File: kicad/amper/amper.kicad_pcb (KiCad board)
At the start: 2 copper layers, 45 parts, among them J1 Conn_01x05, J2 Conn_01x02, J3 Conn_01x15, J4 Conn_01x10, J5 Conn_01x10, Q1 FDS9435A, Q2 FDS9435A, SW1 SW_Push, SW2 SW_Push, SW3 SW_Push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

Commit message: amper rev a
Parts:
- added svg2mod: G***, amper:iridyne_logo, B.Cu at (97.5, 28.6)
- added svg2mod: G***, amper:iridyne_logo, F.Cu at (97.5, 28.6)
- U1: value TM1637 -> UA741CP; footprint amper:TM1637 -> amper:114-87-308-41-134161
- U5: value UA741CP -> TM1637; footprint amper:114-87-308-41-134161 -> amper:TM1637
- moved TP1 162.8 mm to (27.2, 20.9)
- moved R9 153.8 mm to (34.5, 18.6)
- moved R7 153.5 mm to (34.5, 20.9), turned to 180 degrees
- moved TP3 151.2 mm to (35.4, 16.1)
- moved TP5 149.6 mm to (44.3, 16.1)
- moved R6 149.3 mm to (30.1, 59.1), turned to 270 degrees
- moved C5 148.6 mm to (34.5, 25.5), turned to 180 degrees
- moved TP2 148.3 mm to (27.2, 36.1)
- moved C2 146.8 mm to (31.8, 59.1), turned to 90 degrees
- moved TP4 146.1 mm to (35.4, 31.3)
- moved R13 144.4 mm to (46.6, 21.1), turned to 270 degrees
- moved TP6 143.8 mm to (44.3, 31.3)
- moved C6 143.3 mm to (34.5, 40.7), turned to 180 degrees
- moved R10 141.0 mm to (34.5, 23.2), turned to 180 degrees
- moved R8 140.5 mm to (34.5, 36.1), turned to 180 degrees
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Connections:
- SW1 pad 1: /SourceBUp -> /SourceAUp
- SW2 pad 1: /SourceBDn -> /SourceADn
- SW3 pad 1: /SourceAUp -> /SourceBUp
- SW4 pad 1: /SourceADn -> /SourceBDn
- U1 pad 1: GND -> Net-(U1-Pad1)
- U1 pad 2: /SEG1 -> Net-(J2-Pad2)
- U1 pad 3: /SEG2 -> Net-(J2-Pad1)
- U1 pad 4: /SEG3 -> GND
- U1 pad 5: /SEG4 -> Net-(U1-Pad5)
- U1 pad 6: /SEG5 -> /AmpOut
- U1 pad 7: /SEG6 -> +5V
- U1 pad 8: /SEG7 -> Net-(U1-Pad8)
- U3 pad 10: /SourceBDigit1 -> /SourceADigit1
- U3 pad 5: /SourceBDigit2 -> /SourceADigit2
- U4 pad 10: /SourceADigit1 -> /SourceBDigit1
- U4 pad 5: /SourceADigit2 -> /SourceBDigit2
- U5 pad 1: Net-(U5-Pad1) -> GND
- U5 pad 2: Net-(J2-Pad1) -> /SEG1
- U5 pad 3: Net-(J2-Pad2) -> /SEG2
- U5 pad 4: GND -> /SEG3
- U5 pad 5: Net-(U5-Pad5) -> /SEG4
- U5 pad 6: /AmpOut -> /SEG5
- U5 pad 7: +5V -> /SEG6
- U5 pad 8: Net-(U5-Pad8) -> /SEG7
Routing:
- net GND: track 0.00 -> 302.6 mm, vias 0 -> 8
- net +5V: track 0.00 -> 272.9 mm, vias 0 -> 9
- net /SourceA: track 0.00 -> 239.8 mm, vias 0 -> 1
- net /SourceB: track 0.00 -> 194.2 mm, vias 0 -> 1
- net /SEG4: track 0.00 -> 166.4 mm, vias 0 -> 4
- net /AmpOut: track 0.00 -> 165.8 mm
- net /SEG3: track 0.00 -> 163.5 mm, vias 0 -> 4
- net /SEG2: track 0.00 -> 161.2 mm, vias 0 -> 4
- net /SEG1: track 0.00 -> 157.7 mm, vias 0 -> 4
- net /SEG8: track 0.00 -> 151.3 mm, vias 0 -> 4
- net /SEG7: track 0.00 -> 151.0 mm, vias 0 -> 4
- net /SEG6: track 0.00 -> 149.2 mm, vias 0 -> 4
- net /SEG5: track 0.00 -> 148.1 mm, vias 0 -> 4
- net /SourceAPWM: track 0.00 -> 142.8 mm, vias 0 -> 1
- net /SourceBDigit1: track 0.00 -> 130.2 mm, vias 0 -> 2
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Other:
- board outline added: 91.4 x 91.4 mm
- board text added: "5V"
- board text added: "A"
- board text added: "ADn"
- board text added: "APwm"
- board text added: "AUp"
- board text added: "Amper Rev A"
- board text added: "B"
- board text added: "BDn"
- board text added: "BPwm"
- board text added: "BUp"
- board text added: "CLK"
- board text added: "DIO"
- board text added: "GND"
- board text added: "Out"
- board text added: "V"

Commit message: Amper rev A ready to go
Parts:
- removed the svg2mod at (97.5, 28.6) (x2)
- added svg2mod: G***, amper:pcb_logo, B.Cu at (98.0, 28.8)
- added svg2mod: G***, amper:pcb_logo, F.Cu at (98.0, 28.8)
- U1: value UA741CP -> 114-87-308-41-134161

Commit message: Reannotated everything
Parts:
- removed C1, C2: 100pF, Capacitor_SMD:C_0603_1608Metric_Pad1.05x0.95mm_HandSolder
- removed C3: 100nF, Capacitor_SMD:C_0603_1608Metric_Pad1.05x0.95mm_HandSolder
- removed C4: 10uF, Capacitor_SMD:C_0603_1608Metric_Pad1.05x0.95mm_HandSolder
- removed C5, C6, C7, C8: 1u, Capacitor_SMD:C_0603_1608Metric_Pad1.05x0.95mm_HandSolder
- removed J1: Conn_01x05, amper:2.54_2x5_col_ganged
- removed J2: Conn_01x02, amper:2.54_2x5_row_ganged
- removed J3: Conn_01x15, Connector_PinSocket_2.54mm:PinSocket_1x15_P2.54mm_Vertical
- removed J4, J5: Conn_01x10, Connector_PinSocket_2.54mm:PinSocket_1x10_P2.54mm_Vertical
- removed Q1, Q2: FDS9435A, Package_SO:SOIC-8_3.9x4.9mm_P1.27mm
- removed R1, R2, R3, R4, R5, R6: 10K, Resistor_SMD:R_0603_1608Metric_Pad1.05x0.95mm_HandSolder
- removed R10, R12: 40k, Resistor_SMD:R_0603_1608Metric_Pad1.05x0.95mm_HandSolder
- removed R11, R9: 25k, Resistor_SMD:R_0603_1608Metric_Pad1.05x0.95mm_HandSolder
- removed R13, R14: 100K, Resistor_SMD:R_0603_1608Metric_Pad1.05x0.95mm_HandSolder
- removed R7, R8: 60k, Resistor_SMD:R_0603_1608Metric_Pad1.05x0.95mm_HandSolder
- removed SW1, SW2, SW3, SW4: SW_Push, amper:K2-1157SP-I4SW-01
- removed TP1, TP2, TP3, TP4, TP5, TP6: TestPoint, TestPoint:TestPoint_Pad_D2.0mm
- removed U1: 114-87-308-41-134161, amper:114-87-308-41-134161
- removed U2, U3, U4: HDSM-441B, amper:SLS0392FB4A1GD
- removed U5: TM1637, amper:TM1637
- removed U6: ATtiny40-SU, Package_SO:SOIC-20W_7.5x12.8mm_P1.27mm
- removed svg2mod (x2): G***, amper:pcb_logo
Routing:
- net GND: track 302.6 -> 0.00 mm, vias 8 -> 0
- net +5V: track 272.9 -> 0.00 mm, vias 9 -> 0
- net /SourceA: track 239.8 -> 0.00 mm, vias 1 -> 0
- net /SourceB: track 194.2 -> 0.00 mm, vias 1 -> 0
- net /SEG4: track 166.4 -> 0.00 mm, vias 4 -> 0
- net /AmpOut: track 165.8 -> 0.00 mm
- net /SEG3: track 163.5 -> 0.00 mm, vias 4 -> 0
- net /SEG2: track 161.2 -> 0.00 mm, vias 4 -> 0
- net /SEG1: track 157.7 -> 0.00 mm, vias 4 -> 0
- net /SEG8: track 151.3 -> 0.00 mm, vias 4 -> 0
- net /SEG7: track 151.0 -> 0.00 mm, vias 4 -> 0
- net /SEG6: track 149.2 -> 0.00 mm, vias 4 -> 0
- net /SEG5: track 148.1 -> 0.00 mm, vias 4 -> 0
- net /SourceAPWM: track 142.8 -> 0.00 mm, vias 1 -> 0
- net /SourceBDigit1: track 130.2 -> 0.00 mm, vias 2 -> 0
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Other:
- board size 91.4 x 91.4 mm -> 100 x 100 mm
- board text removed: "5V"
- board text removed: "A"
- board text removed: "ADn"
- board text removed: "APwm"
- board text removed: "AUp"
- board text removed: "Amper Rev A"
- board text removed: "B"
- board text removed: "BDn"
- board text removed: "BPwm"
- board text removed: "BUp"
- board text removed: "CLK"
- board text removed: "DIO"
- board text removed: "GND"
- board text removed: "Out"
- board text removed: "V"

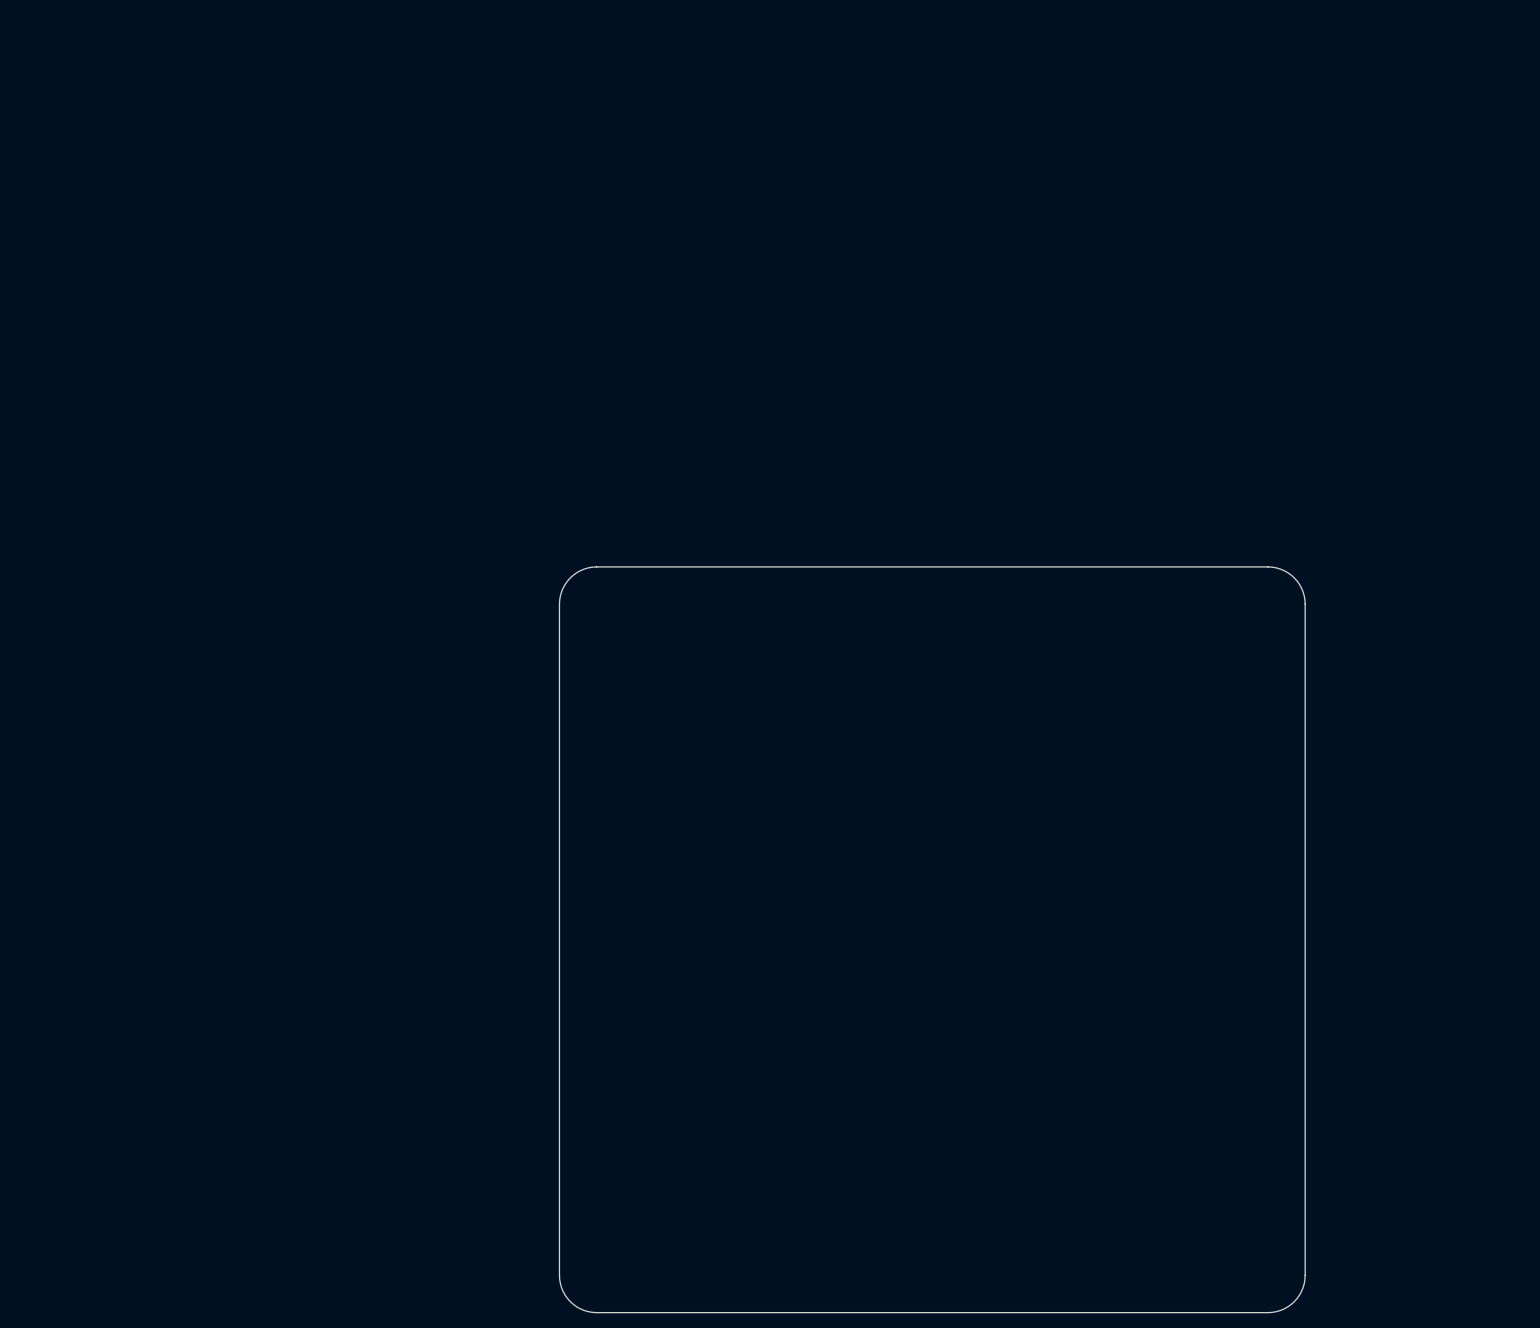
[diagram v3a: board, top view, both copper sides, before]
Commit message: most of the large components in place, started laying tracks
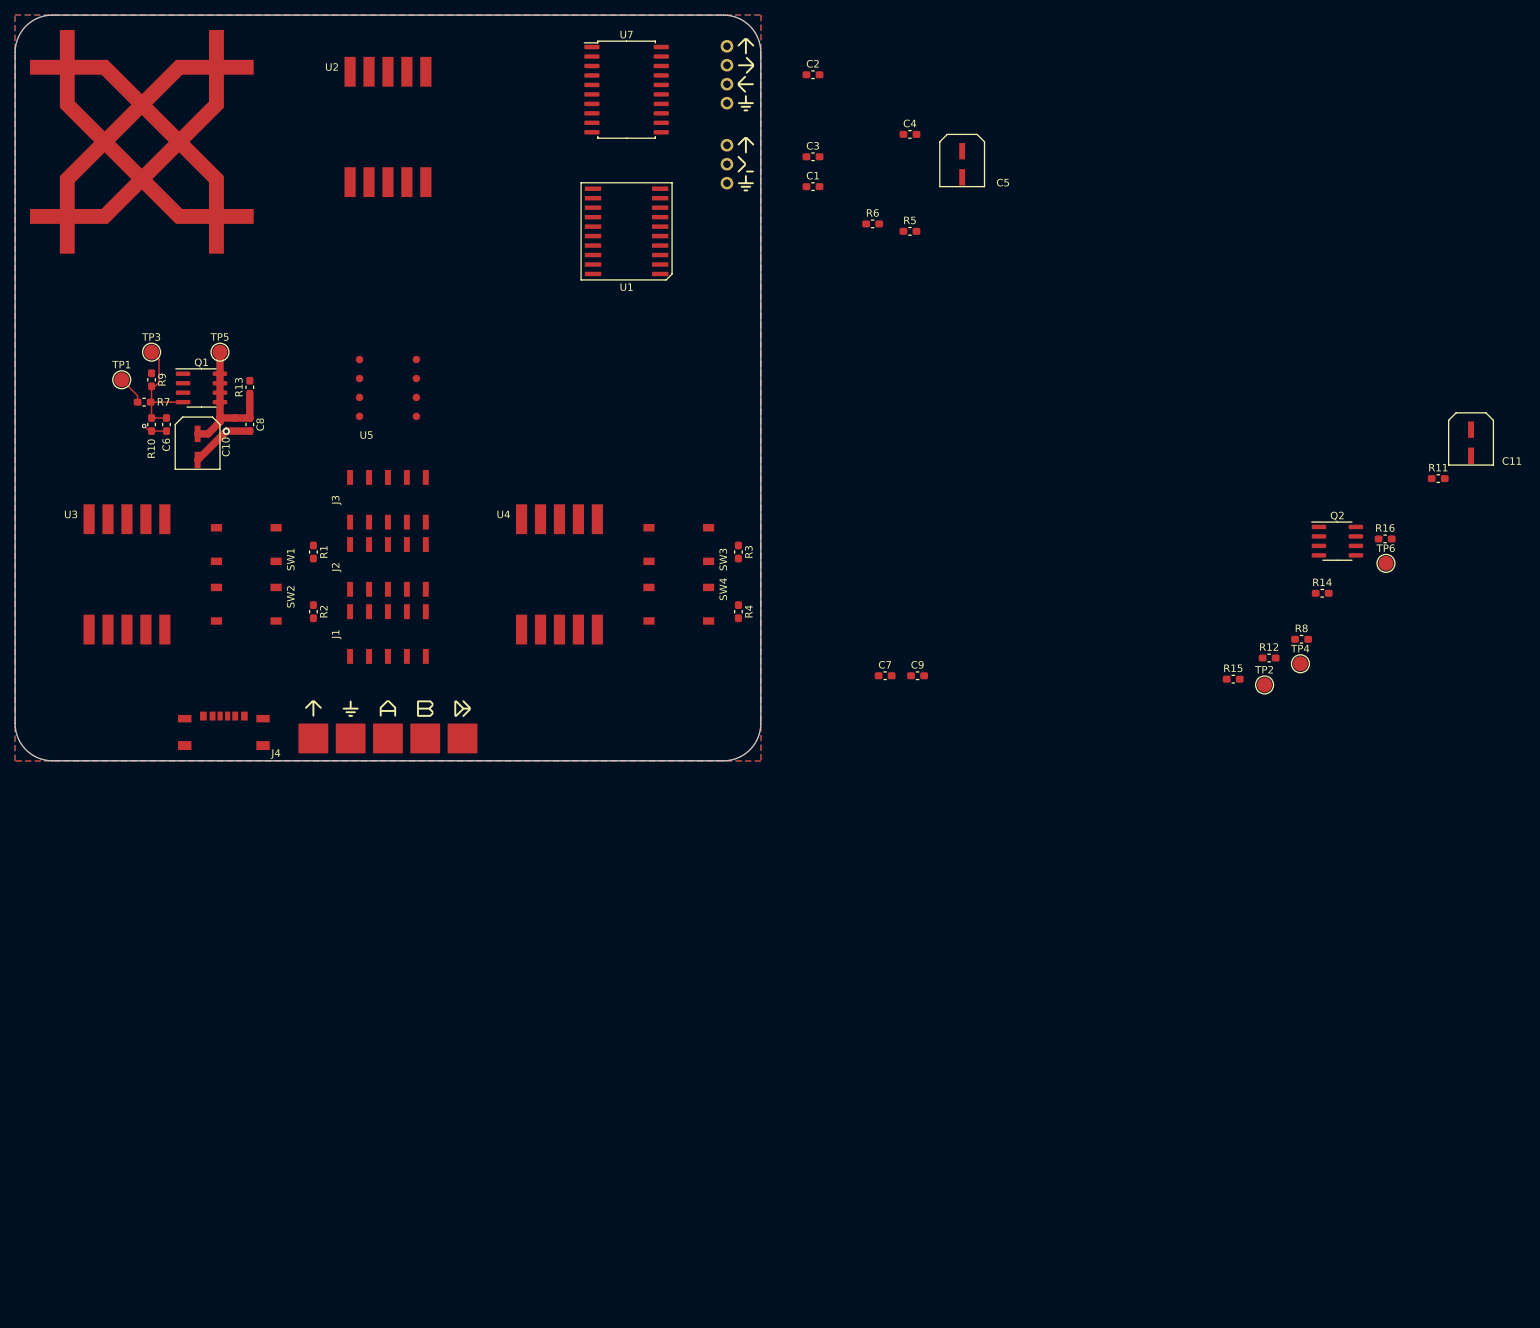
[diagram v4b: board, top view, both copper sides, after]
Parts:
- added C1: 100pF, Capacitor_SMD:C_0603_1608Metric_Pad1.05x0.95mm_HandSolder, F.Cu at (57.0, -27.0)
- added C10: 10uF, amper:VT1H100M-CRD54, F.Cu at (-25.5, 7.91)
- added C11: 10uF, amper:VT1H100M-CRD54, F.Cu at (145.2, 7.34)
- added C2: 100pF, Capacitor_SMD:C_0603_1608Metric_Pad1.05x0.95mm_HandSolder, F.Cu at (57.0, -42.0)
- added C3: 100nF, Capacitor_SMD:C_0603_1608Metric_Pad1.05x0.95mm_HandSolder, F.Cu at (57.0, -31.0)
- added C4: 2uF, Capacitor_SMD:C_0603_1608Metric_Pad1.05x0.95mm_HandSolder, F.Cu at (70.0, -34.0)
- added C5: 10uF, amper:VT1H100M-CRD54, F.Cu at (77.0, -30.0)
- added C6: 1u, Capacitor_SMD:C_0603_1608Metric_Pad1.05x0.95mm_HandSolder, F.Cu at (-29.7, 4.91)
- added C7: 1u, Capacitor_SMD:C_0603_1608Metric_Pad1.05x0.95mm_HandSolder, F.Cu at (66.7, 38.6)
- added C8: 1u, Capacitor_SMD:C_0603_1608Metric_Pad1.05x0.95mm_HandSolder, F.Cu at (-18.5, 4.91)
- added C9: 1u, Capacitor_SMD:C_0603_1608Metric_Pad1.05x0.95mm_HandSolder, F.Cu at (71.0, 38.6)
- added J1: Conn_02x05_Odd_Even, amper:2.54_2x5_alternate, F.Cu at (0.00, 33.0)
- added J2: Conn_02x05_Odd_Even, amper:2.54_2x5_alternate, F.Cu at (0.00, 24.0)
- added J3: Conn_02x05_Odd_Even, amper:2.54_2x5_alternate, F.Cu at (0.00, 15.0)
- added J4: USB_C_Receptacle_USB2.0, amper:MC-303S, F.Cu at (-22.0, 44.0)
- added J5: Conn_01x03, amper:PROG, F.Cu at (48.0, -30.0)
- added J6: Conn_01x04, amper:UART, F.Cu at (48.0, -42.0)
- added J7: Conn_01x05, amper:SolderHeader, F.Cu at (0.00, 42.8)
- added Q1: FDS9435A, Package_SO:SOIC-8_3.9x4.9mm_P1.27mm, F.Cu at (-25.0, 0.00)
- added Q2: FDS9435A, Package_SO:SOIC-8_3.9x4.9mm_P1.27mm, F.Cu at (127.3, 20.5)
- added R1: 10K, Resistor_SMD:R_0603_1608Metric_Pad1.05x0.95mm_HandSolder, F.Cu at (-10.0, 22.0)
- added R10: 20k, Resistor_SMD:R_0603_1608Metric_Pad1.05x0.95mm_HandSolder, F.Cu at (-31.7, 4.91)
- added R11: 12k, Resistor_SMD:R_0603_1608Metric_Pad1.05x0.95mm_HandSolder, F.Cu at (140.8, 12.2)
- added R12: 20k, Resistor_SMD:R_0603_1608Metric_Pad1.05x0.95mm_HandSolder, F.Cu at (118.2, 36.2)
- added R13: 100K, Resistor_SMD:R_0603_1608Metric_Pad1.05x0.95mm_HandSolder, F.Cu at (-18.5, -0.10)
- added R14: 100K, Resistor_SMD:R_0603_1608Metric_Pad1.05x0.95mm_HandSolder, F.Cu at (125.3, 27.5)
- added R15: 4.7K, Resistor_SMD:R_0603_1608Metric_Pad1.05x0.95mm_HandSolder, F.Cu at (113.4, 39.1)
- added R16: 4.7K, Resistor_SMD:R_0603_1608Metric_Pad1.05x0.95mm_HandSolder, F.Cu at (133.7, 20.2)
- added R2: 10K, Resistor_SMD:R_0603_1608Metric_Pad1.05x0.95mm_HandSolder, F.Cu at (-10.0, 30.0)
- added R3: 10K, Resistor_SMD:R_0603_1608Metric_Pad1.05x0.95mm_HandSolder, F.Cu at (47.0, 22.0)
- added R4: 10K, Resistor_SMD:R_0603_1608Metric_Pad1.05x0.95mm_HandSolder, F.Cu at (47.0, 30.0)
- added R5: 10K, Resistor_SMD:R_0603_1608Metric_Pad1.05x0.95mm_HandSolder, F.Cu at (70.0, -21.0)
- added R6: 10K, Resistor_SMD:R_0603_1608Metric_Pad1.05x0.95mm_HandSolder, F.Cu at (65.0, -22.0)
- added R7: 30k, Resistor_SMD:R_0603_1608Metric_Pad1.05x0.95mm_HandSolder, F.Cu at (-32.7, 1.91)
- added R8: 30k, Resistor_SMD:R_0603_1608Metric_Pad1.05x0.95mm_HandSolder, F.Cu at (122.5, 33.7)
- added R9: 12k, Resistor_SMD:R_0603_1608Metric_Pad1.05x0.95mm_HandSolder, F.Cu at (-31.7, -1.09)
- added SW1: SW_Push, amper:K2-1157SP-I4SW-01, F.Cu at (-19.0, 21.0)
- added SW2: SW_Push, amper:K2-1157SP-I4SW-01, F.Cu at (-19.0, 29.0)
- added SW3: SW_Push, amper:K2-1157SP-I4SW-01, F.Cu at (39.0, 21.0)
- added SW4: SW_Push, amper:K2-1157SP-I4SW-01, F.Cu at (39.0, 29.0)
- added TP1: TestPoint, TestPoint:TestPoint_Pad_D2.0mm, F.Cu at (-35.7, -1.09)
- added TP2: TestPoint, TestPoint:TestPoint_Pad_D2.0mm, F.Cu at (117.6, 39.8)
- added TP3: TestPoint, TestPoint:TestPoint_Pad_D2.0mm, F.Cu at (-31.7, -4.80)
- added TP4: TestPoint, TestPoint:TestPoint_Pad_D2.0mm, F.Cu at (122.4, 37.0)
- added TP5: TestPoint, TestPoint:TestPoint_Pad_D2.0mm, F.Cu at (-22.5, -4.80)
- added TP6: TestPoint, TestPoint:TestPoint_Pad_D2.0mm, F.Cu at (133.8, 23.5)
- added U1: TM1637, amper:TM1637, F.Cu at (32.0, -21.0)
- added U2: HDSM-441B, amper:SLS0392FB4A1GD, F.Cu at (0.00, -35.0)
- added U3: HDSM-441B, amper:SLS0392FB4A1GD, F.Cu at (-35.0, 25.0)
- added U4: HDSM-441B, amper:SLS0392FB4A1GD, F.Cu at (23.0, 25.0)
- added U5: 114-87-308-41-134161, amper:114-87-308-41-134161, F.Cu at (0.00, 0.00)
- added U7: ATtiny1606-S, Package_SO:SOIC-20W_7.5x12.8mm_P1.27mm, F.Cu at (32.0, -40.0)
- added svg2mod: G***, amper:pcb_logo, F.Cu at (-33.0, -33.0)
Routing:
- net /SourceAOut: track 0.00 -> 20.3 mm
- net Net-(C6-Pad1): track 0.00 -> 16.4 mm
- net GND: track 0.00 -> 11.9 mm, vias 0 -> 2
- net /SourceAPwm: track 0.00 -> 3.88 mm
- added copper zone on F.Cu, net +5V
- added copper zone on B.Cu, net GND
